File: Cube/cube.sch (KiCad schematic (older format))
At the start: 59 parts, among them Q1 2N2219

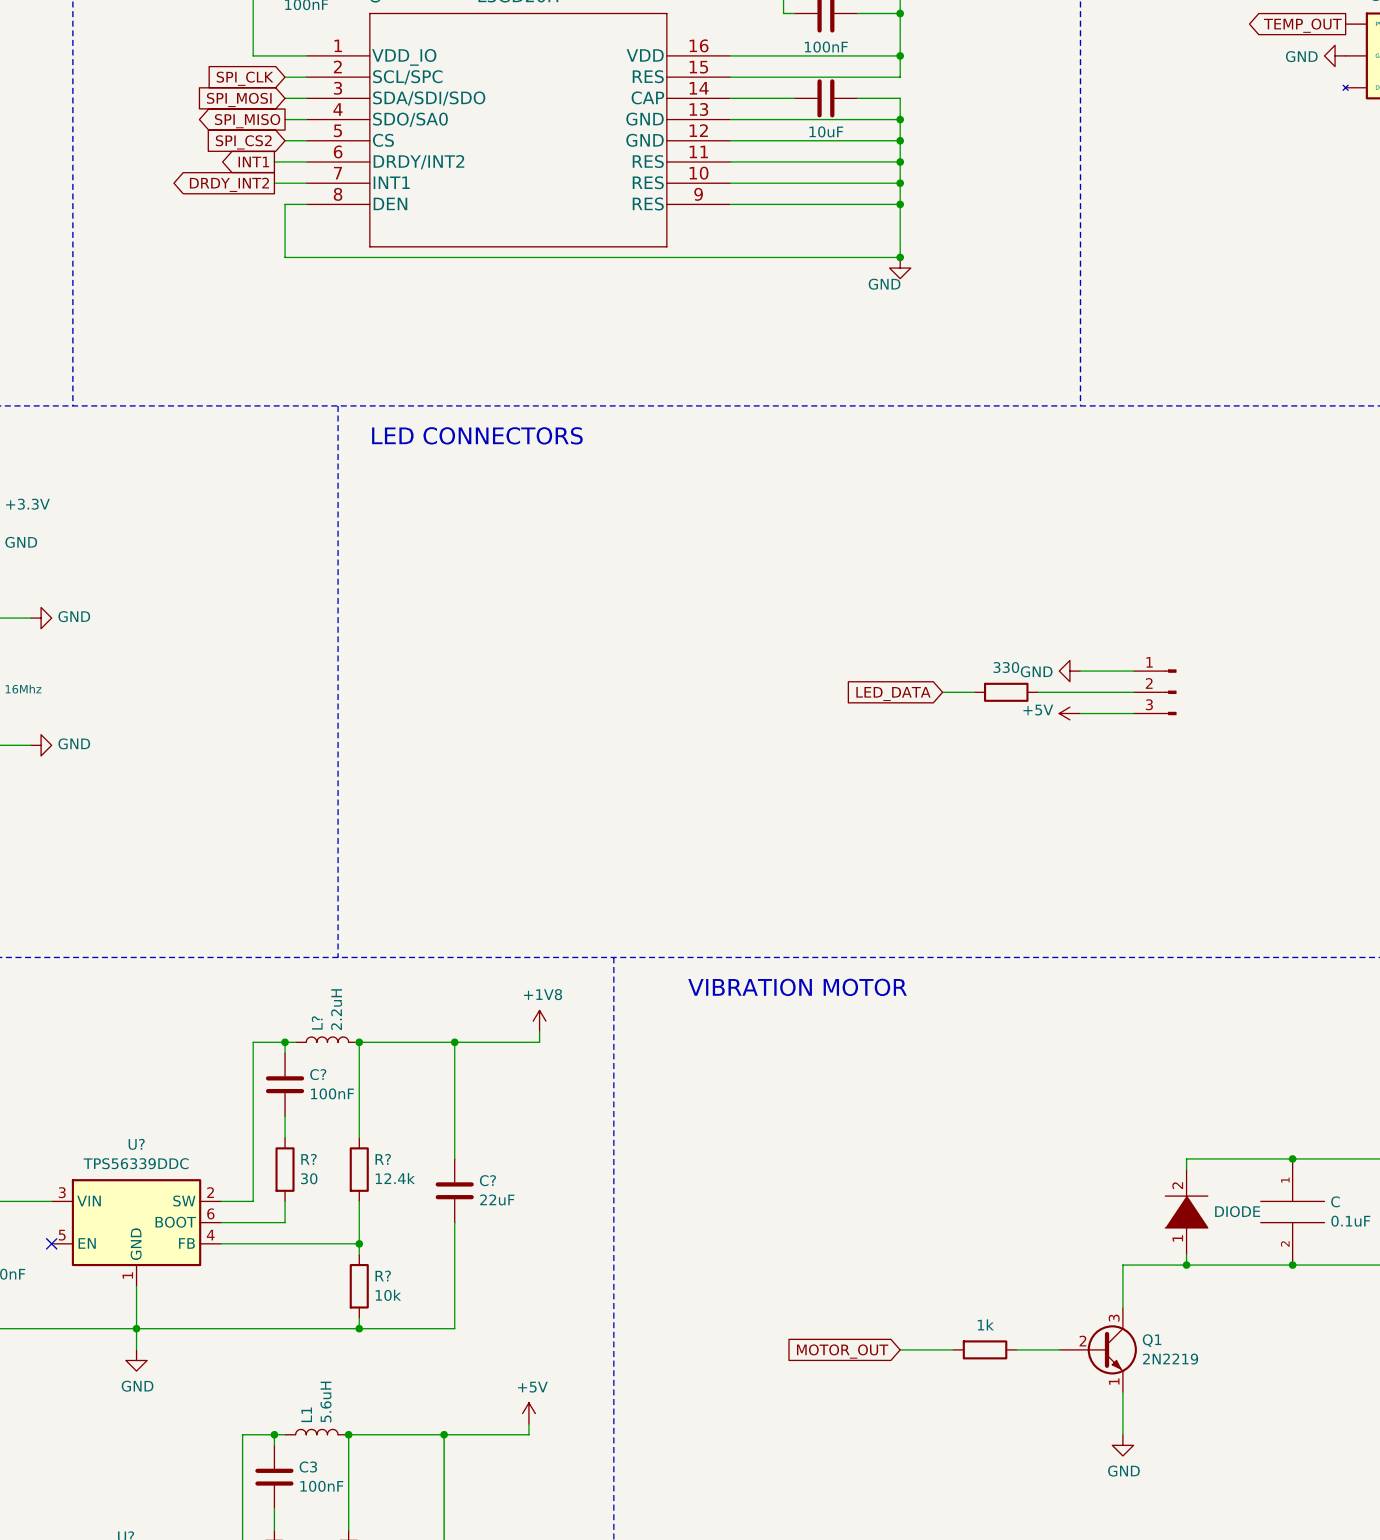
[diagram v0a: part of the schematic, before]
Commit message: Fix minor mistakes after the presentation
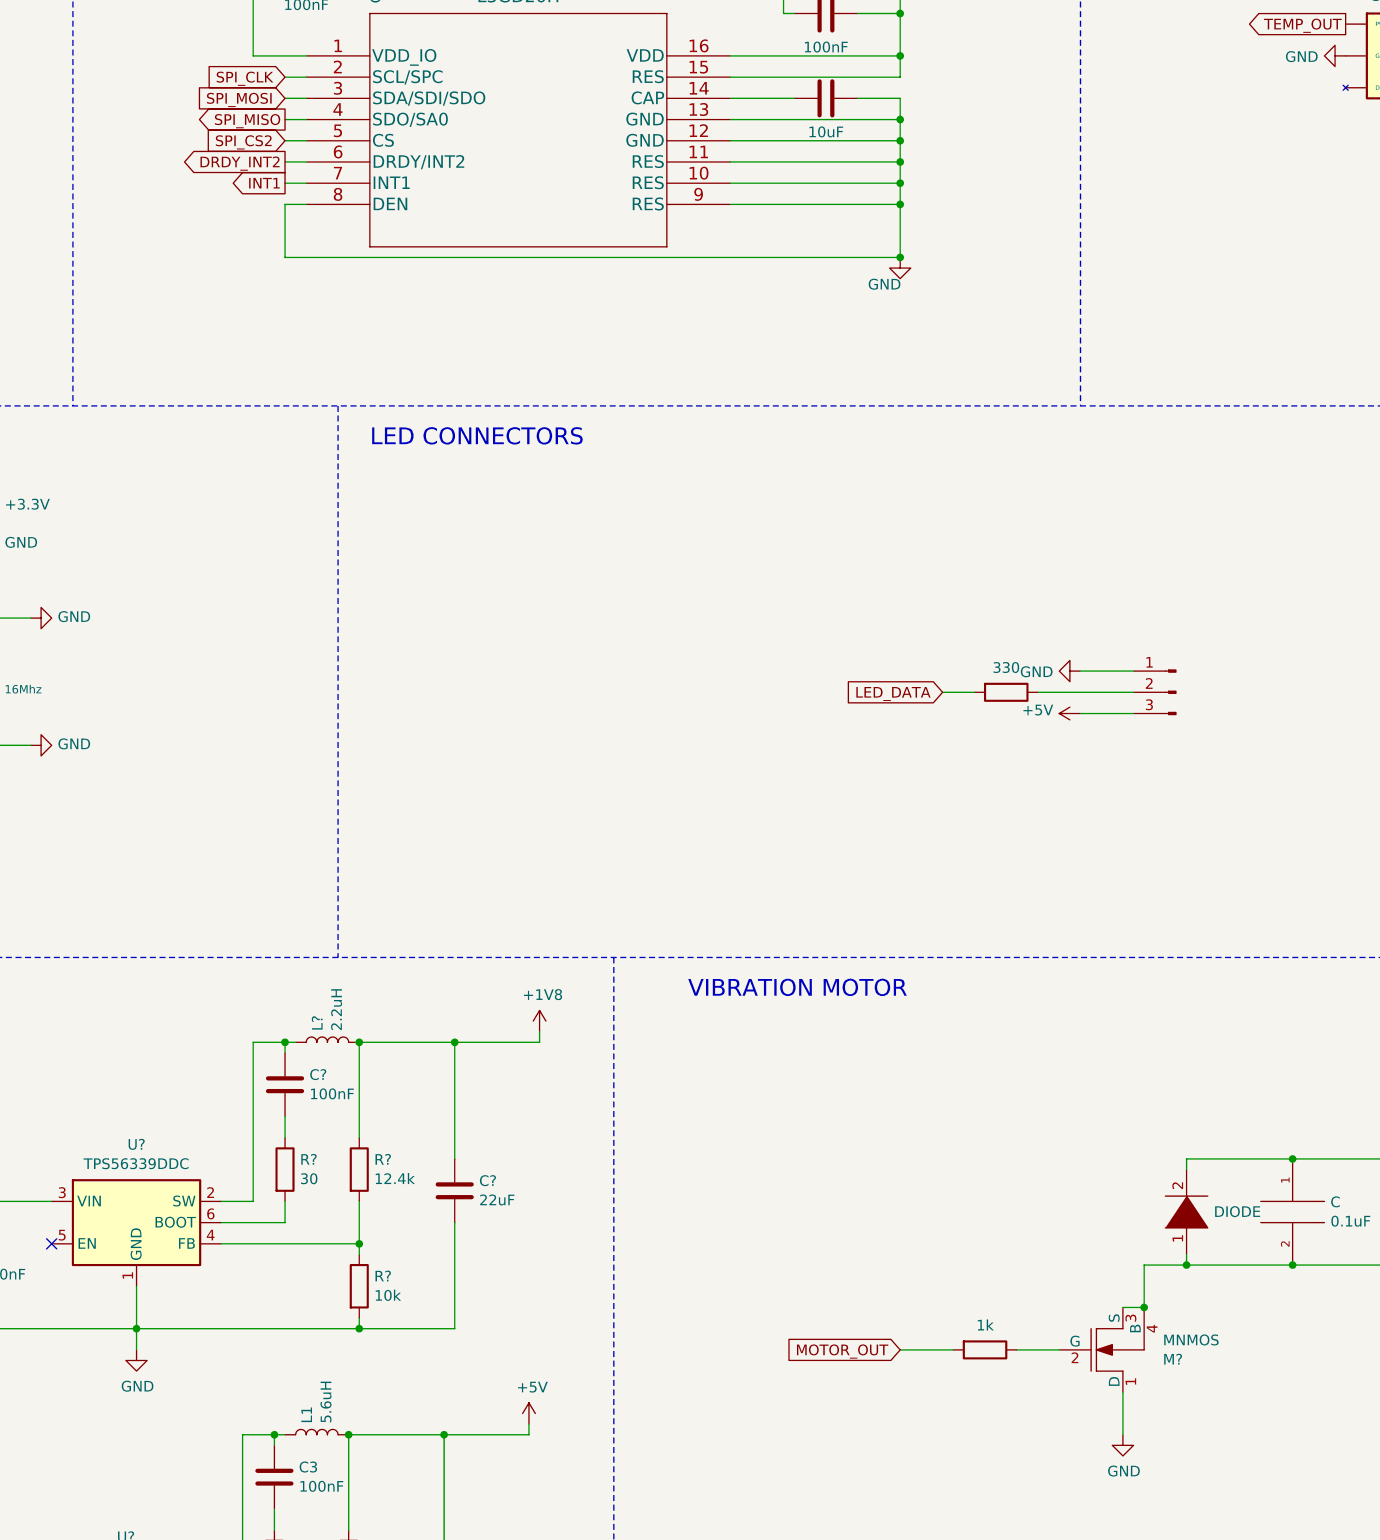
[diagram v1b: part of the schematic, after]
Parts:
- removed L?: 2.2uH, symbol Device:L
- removed Q1: 2N2219, Package_TO_SOT_THT:TO-39-3, symbol Transistor_BJT:2N2219
- added L?: 2.2uH, symbol Device:L
- added M?: MNMOS, symbol pspice:MNMOS
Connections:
- net +1V8: now also L?.2
- net DRDY_INT2: now also U?.6 (DRDY/INT2); no longer U?.7 (INT1)
- net GND: now also M?.1 (D)
- net INT1: now also U?.7 (INT1); no longer U?.6 (DRDY/INT2)
- net at C.2, D?.1 (K), Motor.2 (V-): now also M?.3 (S), M?.4 (B)
- net at C?.1, U?.2 (SW): now also L?.1
- net at 1k.1: now also M?.2 (G)
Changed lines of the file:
@@
 	9650 3200 12550 3200
 Connection ~ 12550 3200
-Text GLabel 9600 2750 0    50   Output ~ 0
+Text GLabel 9650 2850 0    50   Output ~ 0
 INT1
-Wire Wire Line
-	9600 2750 9750 2750
-Text GLabel 9600 2850 0    50   Output ~ 0
+Text GLabel 9650 2750 0    50   Output ~ 0
 DRDY_INT2
-Wire Wire Line
-	9600 2850 9750 2850
 $Comp
 L Connector:Conn_01x03_Male J?
@@
 	1    0    0    -1
 $EndComp
-$Comp
-L Transistor_BJT:2N2219 Q1
-U 1 1 6093CC67
-P 13500 8350
-F 0 "Q1" H 13690 8396 50  0000 L CNN
-F 1 "2N2219" H 13690 8305 50  0000 L CNN
-F 2 "Package_TO_SOT_THT:TO-39-3" H 13700 8275 50  0001 L CIN
-F 3 "http://www.onsemi.com/pub_link/Collateral/2N2219-D.PDF" H 13500 8350 50  0001 L CNN
-	1    13500 8350
-	1    0    0    -1
-$EndComp
-Wire Wire Line
-	13600 8150 13600 7950
-Wire Wire Line
-	13600 7950 13900 7950
-Connection ~ 13900 7950
 Wire Wire Line
 	13600 8550 13600 8750
@@
 Wire Notes Line
 	6750 10600 6700 10600
+Wire Wire Line
+	9750 2750 9650 2750
+Wire Wire Line
+	9750 2850 9650 2850
+$Comp
+L pspice:MNMOS M?
+U 1 1 608A4C83
+P 13500 8350
+F 0 "M?" H 13788 8396 50  0000 L CNN
+F 1 "MNMOS" H 13788 8305 50  0000 L CNN
+F 2 "" H 13475 8350 50  0001 C CNN
+F 3 "~" H 13475 8350 50  0001 C CNN
+	1    13500 8350
+	1    0    0    1
+$EndComp
+Wire Wire Line
+	13900 7950 13700 7950
+Connection ~ 13900 7950
+Wire Wire Line
+	13700 7950 13700 8150
+Wire Wire Line
+	13600 8150 13700 8150
+Connection ~ 13700 8150
 $EndSCHEMATC

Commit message: hub pcb stuck
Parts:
- gave numbers to parts that had none: 44
- renumbered 1k to 1k1, C to C19, CX to CX1, CX to CX2, C1 to CZ1, C2 to CZ2, C3 to CZ3, Motor to Motor1, PullUp to PullUp1, XTAL to XTAL1

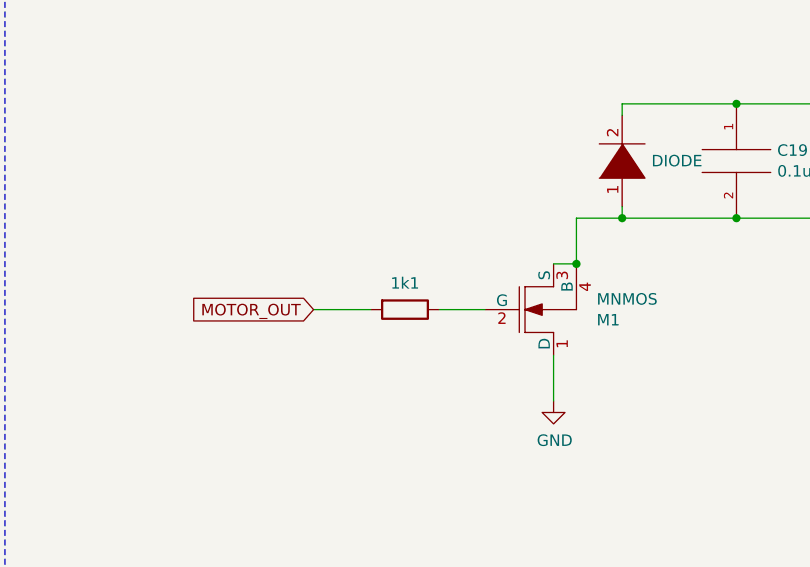
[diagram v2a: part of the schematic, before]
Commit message: Add components to cube
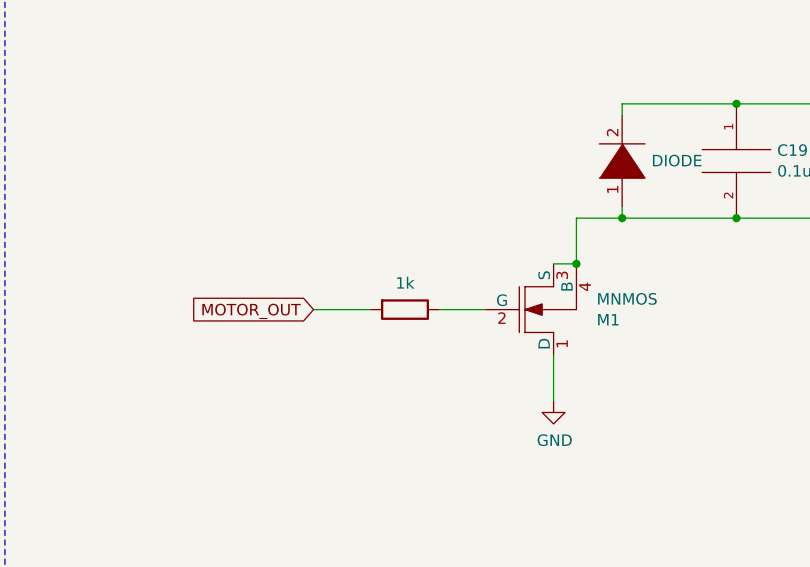
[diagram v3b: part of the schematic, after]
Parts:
- B1: footprint (none) -> RF_Converter:Balun_Johanson_1.6x0.8mm
- C1, C10, C11, C12, C13, C14, C15, C16, C17, C18, C19, C2, C3, C4, C5, C6, C7, C8, C9, CB1, CB2, CB3, CX1, CX2, CZ1, CZ2, CZ3, cb1: footprint (none) -> Capacitor_SMD:C_0603_1608Metric
- D1: footprint (none) -> Diode_SMD:D_0603_1608Metric_Pad1.05x0.95mm_HandSolder
- J1: footprint (none) -> Connector_PinHeader_1.00mm:PinHeader_1x06_P1.00mm_Vertical
- J2: footprint (none) -> Connector_PinHeader_1.00mm:PinHeader_1x03_P1.00mm_Vertical_SMD_Pin1Left
- L1, L2, L3: footprint (none) -> Inductor_SMD:L_0603_1608Metric
- Motor1: footprint XDCR_C0720B001F -> (none)
- PullUp1, R1, R10, R11, R2, R3, R4, R5, R6, R7, R8, R9: footprint (none) -> Resistor_SMD:R_0603_1608Metric
- U1: footprint PDIP40_P_MCH -> (none)
- U3: footprint 32QN2_ATM -> (none)
- U6: footprint LGA-16_3X3X1_STM -> (none)
- W3043: footprint (none) -> RF_Antenna:Texas_SWRA117D_2.4GHz_Left
- XTAL1: footprint (none) -> Crystal:Crystal_SMD_MicroCrystal_CC4V-T1A-2Pin_5.0x1.9mm
- renumbered 1k1 to 1k

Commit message: Add cube pcb layout
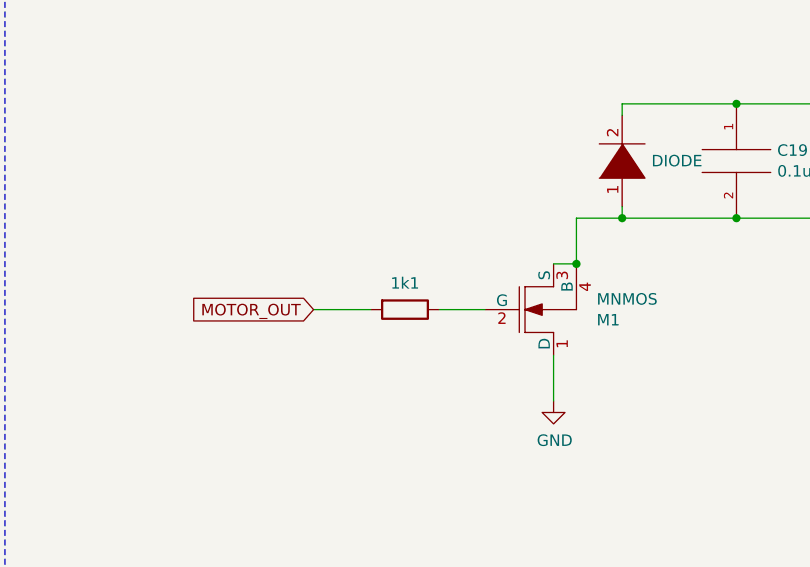
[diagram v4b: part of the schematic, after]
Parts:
- 1k1: renamed from 1k; footprint (none) -> Resistor_SMD:R_0603_1608Metric
- M1: footprint (none) -> Package_TO_SOT_SMD:SOT-23W_Handsoldering
- Motor1: footprint (none) -> VibrationMotorFootprint:XDCR_C0720B001F
- U1: footprint (none) -> PIC18Footprint:PIC18F47K40-I&slash_P
- U3: footprint (none) -> Zigbee:AT86RF231-ZU
- U6: footprint (none) -> Gyroscope:L3GD20H
- U7: footprint (none) -> TempHumFootprint:SON100P300X300X80-7N
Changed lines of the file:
@@
 F 0 "U3" H 5900 4837 60  0001 C CNN
 F 1 "AT86RF231-ZU" H 5900 4731 60  0000 C CNN
-F 2 "" H 5900 4690 60  0001 C CNN
+F 2 "Zigbee:AT86RF231-ZU" H 5900 4690 60  0001 C CNN
 F 3 "" H 5000 4450 60  0000 C CNN
 	1    5000 4450
@@
 F 0 "Motor1" H 15428 7746 50  0000 L CNN
 F 1 "C0720B001F" H 15428 7655 50  0000 L CNN
-F 2 "" H 15200 7700 50  0001 L BNN
+F 2 "VibrationMotorFootprint:XDCR_C0720B001F" H 15200 7700 50  0001 L BNN
 F 3 "" H 15200 7700 50  0001 L BNN
 F 4 "Jinlong Machinery" H 15200 7700 50  0001 L BNN "MF"
@@
 F 0 "U6" H 10750 2637 60  0001 C CNN
 F 1 "L3GD20H" H 10750 2531 60  0000 C CNN
-F 2 "" H 10750 2490 60  0001 C CNN
+F 2 "Gyroscope:L3GD20H" H 10750 2490 60  0001 C CNN
 F 3 "" H 9750 2250 60  0000 C CNN
 	1    9750 2250
@@
 F 0 "U7" H 14970 2625 50  0001 C CNN
 F 1 "Si7007-A20" H 14970 2533 50  0000 C CNN
-F 2 "" H 14750 2500 50  0001 C CNN
+F 2 "TempHumFootprint:SON100P300X300X80-7N" H 14750 2500 50  0001 C CNN
 F 3 "" H 14750 2500 50  0001 C CNN
 	1    14950 2250
@@
 	13300 8350 13100 8350
 $Comp
-L Device:R 1k
+L Device:R 1k1
 U 1 1 60957369
 P 12950 8350
-F 0 "1k" V 12835 8350 50  0000 C CNN
+F 0 "1k1" V 12835 8350 50  0000 C CNN
 F 1 "R" V 12834 8350 50  0001 C CNN
-F 2 "" V 12880 8350 50  0001 C CNN
+F 2 "Resistor_SMD:R_0603_1608Metric" V 12880 8350 50  0001 C CNN
 F 3 "~" H 12950 8350 50  0001 C CNN
 	1    12950 8350
@@
 F 0 "U1" H 3350 1737 60  0001 C CNN
 F 1 "PIC18F47K40-I_P" H 3350 1631 60  0000 C CNN
-F 2 "" H 3350 1590 60  0001 C CNN
+F 2 "PIC18Footprint:PIC18F47K40-I&slash_P" H 3350 1590 60  0001 C CNN
 F 3 "" H 1850 1350 60  0000 C CNN
 	1    1850 1350
@@
 F 0 "M1" H 13788 8396 50  0000 L CNN
 F 1 "MNMOS" H 13788 8305 50  0000 L CNN
-F 2 "" H 13475 8350 50  0001 C CNN
+F 2 "Package_TO_SOT_SMD:SOT-23W_Handsoldering" H 13475 8350 50  0001 C CNN
 F 3 "~" H 13475 8350 50  0001 C CNN
 	1    13500 8350
